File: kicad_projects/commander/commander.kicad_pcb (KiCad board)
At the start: 2 copper layers, 50 x 70 mm, 14 parts, among them J1 Conn_02x07_Odd_Even, J2 Conn_02x07_Odd_Even, J4 TPS pinout, J5 DS1020-12-6VBT1A-R, J6 PSP 3000 connector SFV4R-4STB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, J7 PSP 2000 raw pins out, U1 Pico, U2 FODM3053

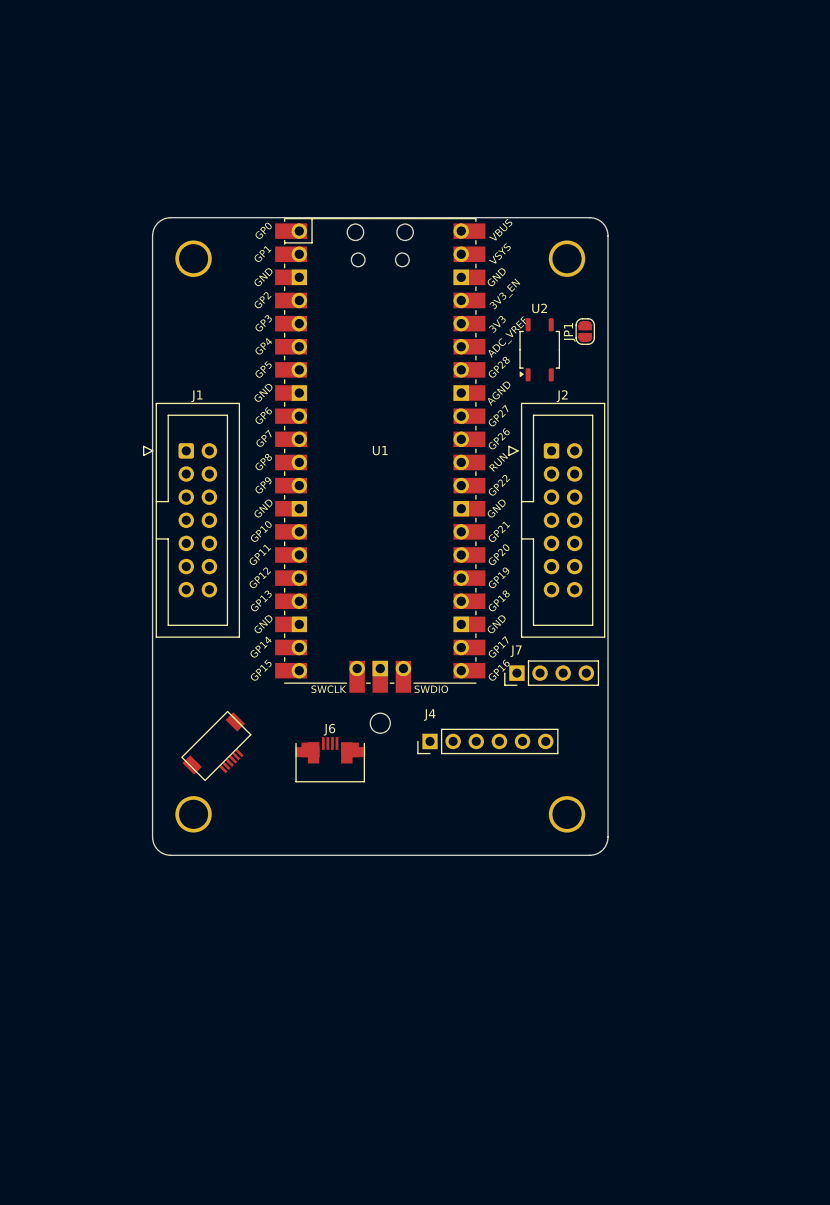
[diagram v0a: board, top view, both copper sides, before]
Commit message: Commander board passing DRC
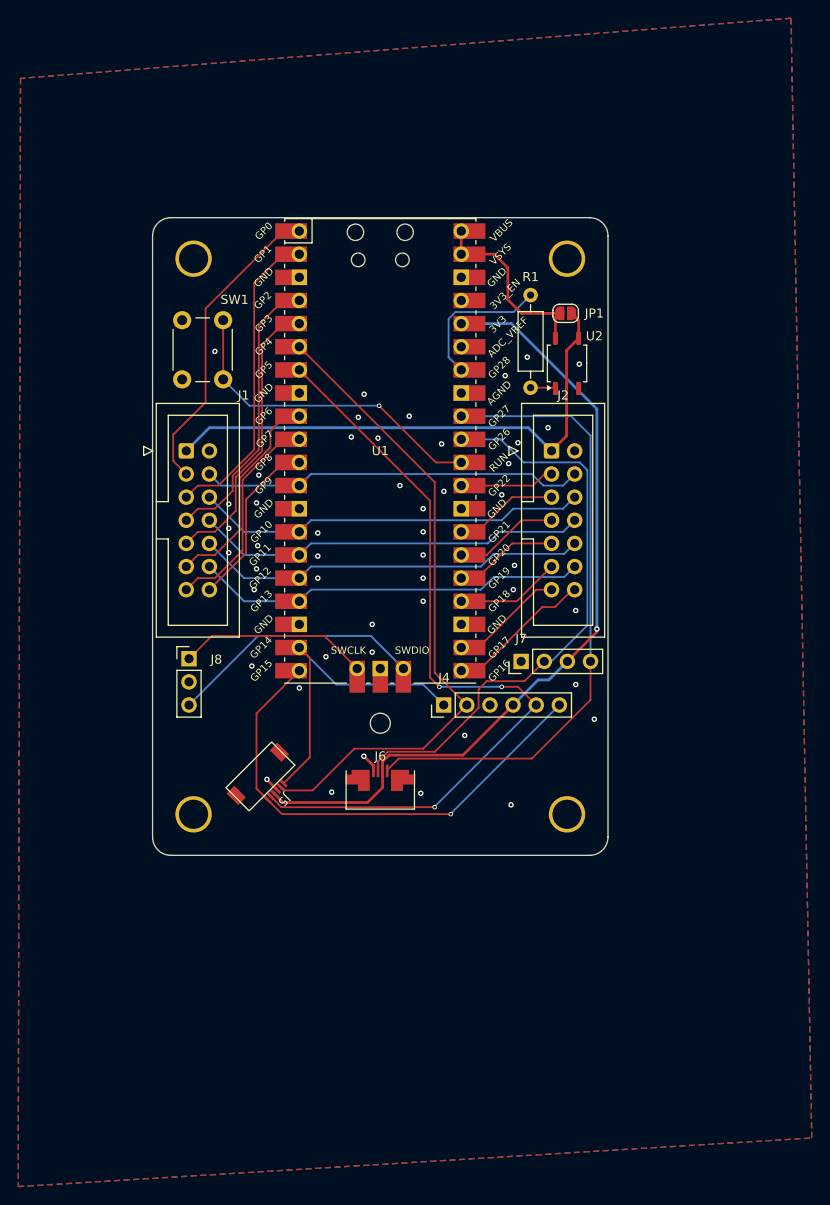
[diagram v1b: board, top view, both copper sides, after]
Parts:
- added J8: debug out, Connector_PinHeader_2.54mm:PinHeader_1x03_P2.54mm_Vertical, F.Cu at (114.0, 108.4)
- added R1: 200R, Resistor_THT:R_Axial_DIN0207_L6.3mm_D2.5mm_P10.16mm_Horizontal, F.Cu at (151.5, 78.7)
- added SW1: RESET_SWITCH, Button_Switch_THT:SW_PUSH_6mm_H4.3mm, F.Cu at (113.2, 77.8)
- J1: value Conn_02x07_Odd_Even -> left input IDC14
- J2: value Conn_02x07_Odd_Even -> right input IDC14
- U2: value FODM3053 -> AQY212S
- moved J6 6.26 mm to (135.0, 120.7)
- moved J5 5.88 mm to (123.5, 123.0)
- moved J4 4.27 mm to (142.0, 113.5)
- moved U2 3.35 mm to (155.5, 76.0)
- moved JP1 2.94 mm to (155.3, 70.5), turned to 0 degrees
- moved J7 1.37 mm to (150.5, 108.7)
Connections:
- J1 pad 1: unconnected-(J1-Pin_1-Pad1) -> LED_5V
- J1 pad 10: unconnected-(J1-Pin_10-Pad10) -> /ROW1
- J1 pad 11: unconnected-(J1-Pin_11-Pad11) -> /COL4
- J1 pad 12: unconnected-(J1-Pin_12-Pad12) -> /ROW0
- J1 pad 13: unconnected-(J1-Pin_13-Pad13) -> /COL5
- J1 pad 14: unconnected-(J1-Pin_14-Pad14) -> /COL6
- J1 pad 2: unconnected-(J1-Pin_2-Pad2) -> GND
- J1 pad 3: unconnected-(J1-Pin_3-Pad3) -> /COL0
- J1 pad 4: unconnected-(J1-Pin_4-Pad4) -> /ROW4
- J1 pad 5: unconnected-(J1-Pin_5-Pad5) -> /COL1
- J1 pad 6: unconnected-(J1-Pin_6-Pad6) -> /ROW3
- J1 pad 7: unconnected-(J1-Pin_7-Pad7) -> /COL2
- J1 pad 8: unconnected-(J1-Pin_8-Pad8) -> /ROW2
- J1 pad 9: unconnected-(J1-Pin_9-Pad9) -> /COL3
- J2 pad 1: unconnected-(J2-Pin_1-Pad1) -> LED_5V
- J2 pad 10: unconnected-(J2-Pin_10-Pad10) -> /ROW1
- J2 pad 11: unconnected-(J2-Pin_11-Pad11) -> /COL11
- J2 pad 12: unconnected-(J2-Pin_12-Pad12) -> /ROW0
- J2 pad 13: unconnected-(J2-Pin_13-Pad13) -> /COL12
- J2 pad 14: unconnected-(J2-Pin_14-Pad14) -> /COL13
- J2 pad 2: unconnected-(J2-Pin_2-Pad2) -> GND
- J2 pad 3: unconnected-(J2-Pin_3-Pad3) -> /COL7
- J2 pad 4: unconnected-(J2-Pin_4-Pad4) -> /ROW4
- J2 pad 5: unconnected-(J2-Pin_5-Pad5) -> /COL8
- J2 pad 6: unconnected-(J2-Pin_6-Pad6) -> /ROW3
- J2 pad 7: unconnected-(J2-Pin_7-Pad7) -> /COL9
- J2 pad 8: unconnected-(J2-Pin_8-Pad8) -> /ROW2
- J2 pad 9: unconnected-(J2-Pin_9-Pad9) -> /COL10
- JP1 pad 1: 5V5 -> 5V
- JP1 pad 2: LED_5V5 -> LED_5V
- U1 pad 1: unconnected-(U1-GPIO0-Pad1) -> /COL0
- U1 pad 10: unconnected-(U1-GPIO7-Pad10) -> /COL5
- U1 pad 11: unconnected-(U1-GPIO8-Pad11) -> /COL6
- U1 pad 12: unconnected-(U1-GPIO9-Pad12) -> /ROW4
- U1 pad 14: unconnected-(U1-GPIO10-Pad14) -> /ROW3
- U1 pad 15: unconnected-(U1-GPIO11-Pad15) -> /ROW2
- U1 pad 16: unconnected-(U1-GPIO12-Pad16) -> /ROW1
- U1 pad 17: unconnected-(U1-GPIO13-Pad17) -> /ROW0
- U1 pad 19: unconnected-(U1-GPIO14-Pad19) -> /TPS_RDY
- U1 pad 2: unconnected-(U1-GPIO1-Pad2) -> /COL1
- U1 pad 20: unconnected-(U1-GPIO15-Pad20) -> /TPS_NRST
- U1 pad 21: unconnected-(U1-GPIO16-Pad21) -> /COL13
- U1 pad 22: unconnected-(U1-GPIO17-Pad22) -> /COL12
- U1 pad 24: unconnected-(U1-GPIO18-Pad24) -> /COL11
- U1 pad 25: unconnected-(U1-GPIO19-Pad25) -> /COL10
- U1 pad 26: unconnected-(U1-GPIO20-Pad26) -> /COL9
- U1 pad 27: unconnected-(U1-GPIO21-Pad27) -> /COL8
- U1 pad 29: unconnected-(U1-GPIO22-Pad29) -> /COL7
- U1 pad 30: unconnected-(U1-RUN-Pad30) -> /RUN
- U1 pad 31: unconnected-(U1-GPIO26_ADC0-Pad31) -> /X1
- U1 pad 32: unconnected-(U1-GPIO27_ADC1-Pad32) -> /X2
- U1 pad 34: unconnected-(U1-GPIO28_ADC2-Pad34) -> /LED_ENABLE
- U1 pad 39: unconnected-(U1-VSYS-Pad39) -> 5V
- U1 pad 4: unconnected-(U1-GPIO2-Pad4) -> /COL2
- U1 pad 40: unconnected-(U1-VBUS-Pad40) -> 5V
- U1 pad 41: unconnected-(U1-SWCLK-Pad41) -> Net-(J8-Pin_1)
- U1 pad 43: unconnected-(U1-SWDIO-Pad43) -> Net-(J8-Pin_3)
- U1 pad 5: unconnected-(U1-GPIO3-Pad5) -> /COL3
- U1 pad 6: unconnected-(U1-GPIO4-Pad6) -> /TPS_SDA
- U1 pad 7: unconnected-(U1-GPIO5-Pad7) -> /TPS_SCL
- U1 pad 9: unconnected-(U1-GPIO6-Pad9) -> /COL4
- U2 pad 1: unconnected-(U2-Pad1) -> Net-(R1-Pad1)
- U2 pad 2: unconnected-(U2-Pad2) -> GND
- U2 pad 3: LED_5V5 -> LED_5V
- U2 pad 4: 5V5 -> 5V
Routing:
- net 3V3: track 0.00 -> 88.5 mm, vias 0 -> 1
- net /TPS_SCL: track 0.00 -> 87.0 mm, vias 0 -> 3
- net /TPS_SDA: track 0.00 -> 71.5 mm
- net /X2: track 0.00 -> 70.5 mm
- net /X1: track 0.00 -> 64.0 mm
- net LED_5V: track 0.00 -> 58.9 mm
- net /TPS_NRST: track 0.00 -> 54.3 mm, vias 0 -> 1
- net /ROW2: track 0.00 -> 43.3 mm
- net /ROW0: track 0.00 -> 43.3 mm
- net /ROW3: track 0.00 -> 43.3 mm
- net /ROW1: track 0.00 -> 43.3 mm
- net /ROW4: track 0.00 -> 42.2 mm
- net /RUN: track 0.00 -> 36.4 mm, vias 0 -> 1
- net /TPS_RDY: track 0.00 -> 35.1 mm
- net /COL1: track 0.00 -> 34.2 mm
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- added copper zone on B.Cu, net GND
- added copper zone on F.Cu, net GND

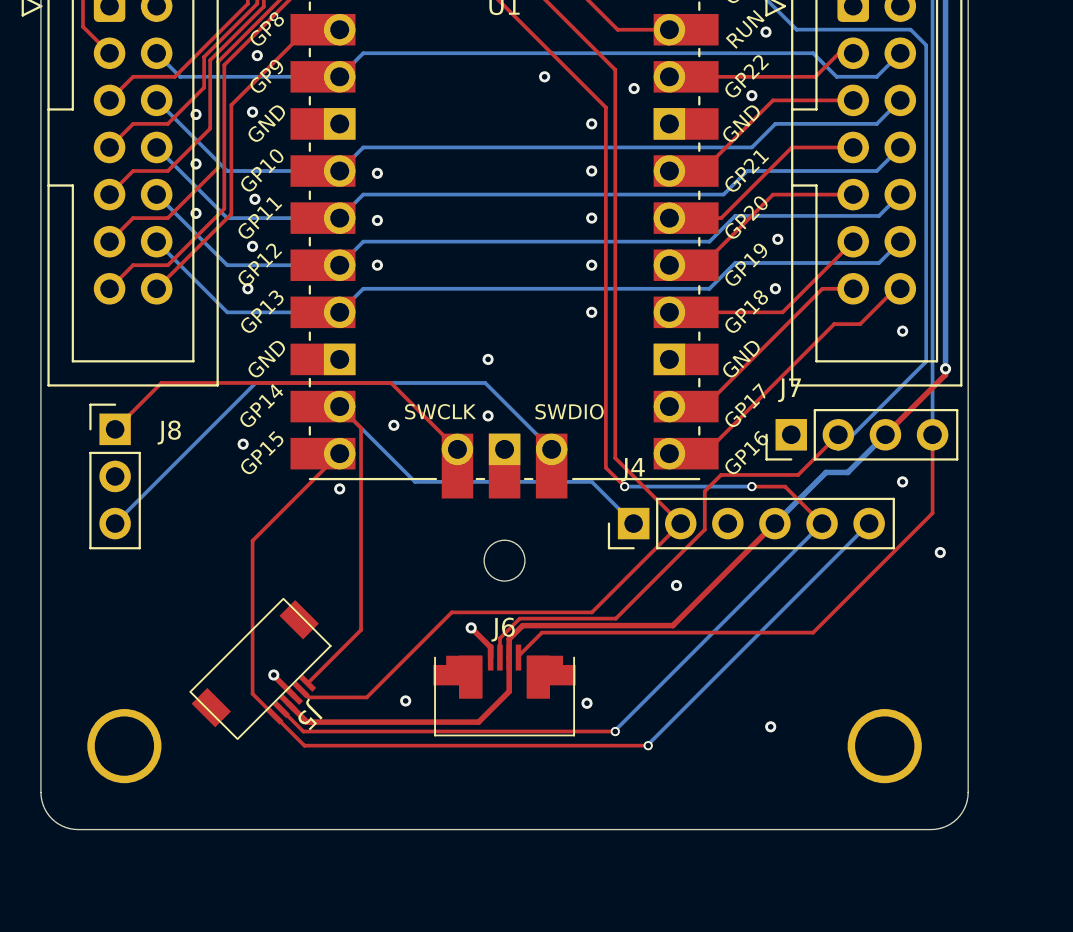
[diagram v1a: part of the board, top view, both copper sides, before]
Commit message: Add silkscreen info, some more routing
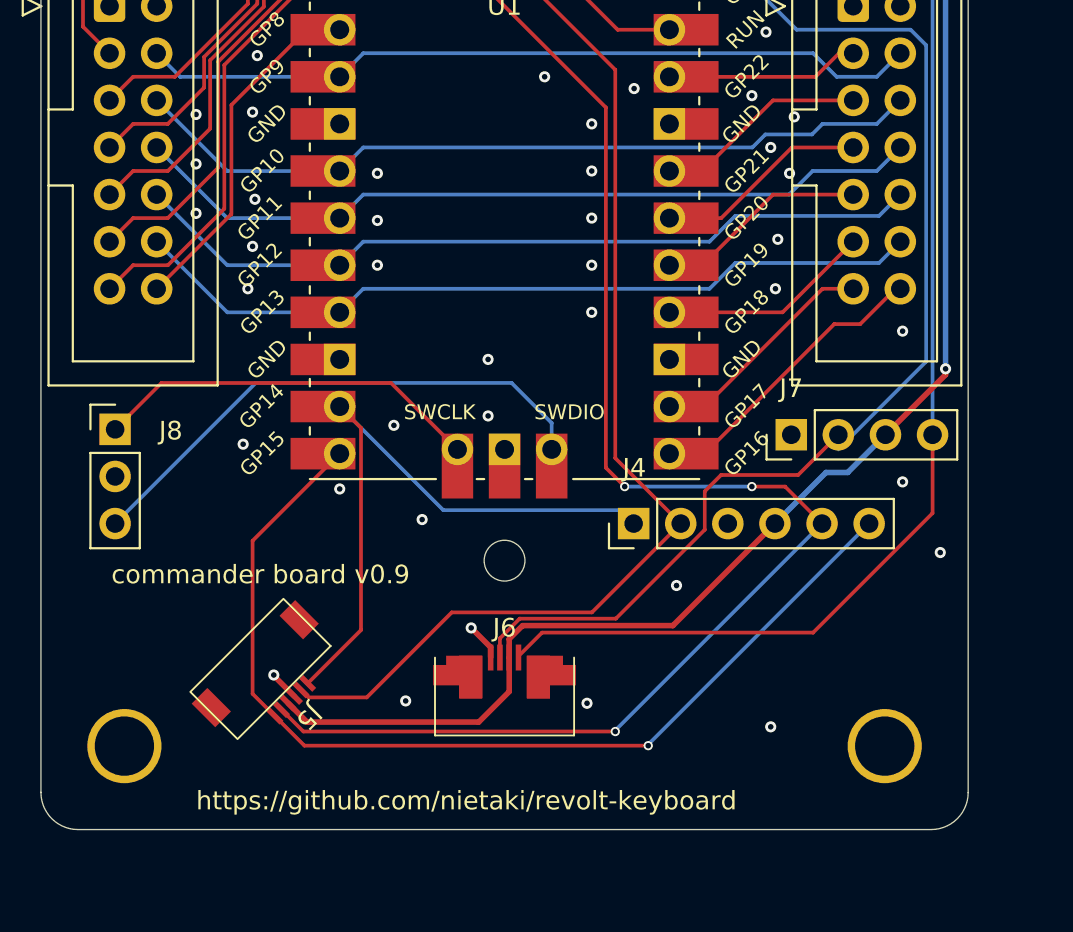
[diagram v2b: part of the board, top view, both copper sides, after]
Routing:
- net Net-(J8-Pin_3): track 28.2 -> 29.0 mm
- net GND: vias 48 -> 52
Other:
- board text added: "commander board v0.9"
- board text added: "https://github.com/nietaki/revolt-keyboard"
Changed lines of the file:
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@@
   (gr_line (start 160 62) (end 160 128)
     (stroke (width 0.05) (type default)) (layer "Edge.Cuts"))
+  (gr_text "https://github.com/nietaki/revolt-keyboard" (at 118.364 129.032) (layer "F.SilkS")
+    (effects (font (size 1 1) (thickness 0.15)) (justify left bottom))
+  )
+  (gr_text "commander board v0.9" (at 113.792 116.84) (layer "F.SilkS")
+    (effects (font (size 1 1) (thickness 0.15)) (justify left bottom))
+  )
   (gr_text "PSP joystick" (at 130.5 130.5) (layer "Dwgs.User")
     (effects (font (size 1 1) (thickness 0.15)) (justify left bottom))
@@
   (segment (start 121.158 85.471) (end 117.221 89.408) (width 0.2) (layer "F.Cu") (net 3))
   (segment (start 121.158 67.183) (end 121.158 85.471) (width 0.2) (layer "F.Cu") (net 3))
-  (segment (start 149.606 91.948) (end 148.336 93.218) (width 0.2) (layer "B.Cu") (net 4))
+  (segment (start 151.576 92.518) (end 149.06205 92.518) (width 0.2) (layer "B.Cu") (net 4))
+  (segment (start 127.382 93.218) (end 126.11 94.49) (width 0.2) (layer "B.Cu") (net 4))
+  (segment (start 149.06205 92.518) (end 148.36205 93.218) (width 0.2) (layer "B.Cu") (net 4))
+  (segment (start 155.072 91.948) (end 152.146 91.948) (width 0.2) (layer "B.Cu") (net 4))
+  (segment (start 152.146 91.948) (end 151.576 92.518) (width 0.2) (layer "B.Cu") (net 4))
   (segment (start 156.34 90.68) (end 155.072 91.948) (width 0.2) (layer "B.Cu") (net 4))
   (segment (start 126.11 94.49) (end 120.05 94.49) (width 0.2) (layer "B.Cu") (net 4))
   (segment (start 120.05 94.49) (end 116.24 90.68) (width 0.2) (layer "B.Cu") (net 4))
-  (segment (start 127.382 93.218) (end 126.11 94.49) (width 0.2) (layer "B.Cu") (net 4))
-  (segment (start 148.336 93.218) (end 127.382 93.218) (width 0.2) (layer "B.Cu") (net 4))
-  (segment (start 155.072 91.948) (end 149.606 91.948) (width 0.2) (layer "B.Cu") (net 4))
+  (segment (start 148.36205 93.218) (end 127.382 93.218) (width 0.2) (layer "B.Cu") (net 4))
   (segment (start 118.799 89.989) (end 116.84 91.948) (width 0.2) (layer "F.Cu") (net 5))
   (segment (start 126.11 69.09) (end 124.331 69.09) (width 0.2) (layer "F.Cu") (net 5))
@@
   (segment (start 116.84 91.948) (end 114.972 91.948) (width 0.2) (layer "F.Cu") (net 5))
   (segment (start 121.666 71.755) (end 121.666 85.471) (width 0.2) (layer "F.Cu") (net 5))
+  (segment (start 127.382 95.758) (end 126.11 97.03) (width 0.2) (layer "B.Cu") (net 6))
+  (segment (start 151.61195 94.488) (end 150.34195 95.758) (width 0.2) (layer "B.Cu") (net 6))
+  (segment (start 150.34195 95.758) (end 127.382 95.758) (width 0.2) (layer "B.Cu") (net 6))
+  (segment (start 120.05 97.03) (end 116.24 93.22) (width 0.2) (layer "B.Cu") (net 6))
+  (segment (start 155.072 94.488) (end 151.61195 94.488) (width 0.2) (layer "B.Cu") (net 6))
   (segment (start 156.34 93.22) (end 155.072 94.488) (width 0.2) (layer "B.Cu") (net 6))
-  (segment (start 148.082 94.488) (end 146.812 95.758) (width 0.2) (layer "B.Cu") (net 6))
-  (segment (start 120.05 97.03) (end 116.24 93.22) (width 0.2) (layer "B.Cu") (net 6))
-  (segment (start 146.812 95.758) (end 127.382 95.758) (width 0.2) (layer "B.Cu") (net 6))
-  (segment (start 155.072 94.488) (end 148.082 94.488) (width 0.2) (layer "B.Cu") (net 6))
   (segment (start 126.11 97.03) (end 120.05 97.03) (width 0.2) (layer "B.Cu") (net 6))
-  (segment (start 127.382 95.758) (end 126.11 97.03) (width 0.2) (layer "B.Cu") (net 6))
   (segment (start 122.018478 73.942522) (end 124.331 71.63) (width 0.2) (layer "F.Cu") (net 7))
   (segment (start 116.84 94.488) (end 119.126 92.202) (width 0.2) (layer "F.Cu") (net 7))
@@
   (segment (start 132.46 109.5) (end 128.878 105.918) (width 0.2) (layer "F.Cu") (net 20))
   (segment (start 116.502 105.918) (end 114 108.42) (width 0.2) (layer "F.Cu") (net 20))
-  (segment (start 133.958 105.918) (end 121.582 105.918) (width 0.2) (layer "B.Cu") (net 21))
   (segment (start 121.582 105.918) (end 114 113.5) (width 0.2) (layer "B.Cu") (net 21))
-  (segment (start 137.54 109.5) (end 133.958 105.918) (width 0.2) (layer "B.Cu") (net 21))
+  (segment (start 137.54 108.076) (end 135.382 105.918) (width 0.2) (layer "B.Cu") (net 21))
+  (segment (start 137.54 109.5) (end 137.54 108.076) (width 0.2) (layer "B.Cu") (net 21))
+  (segment (start 135.382 105.918) (end 121.582 105.918) (width 0.2) (layer "B.Cu") (net 21))
   (segment (start 117.75 71.25) (end 117.75 77.75) (width 0.2) (layer "F.Cu") (net 22))
   (segment (start 134.874 80.645) (end 141.099 86.87) (width 0.2) (layer "F.Cu") (net 22))
@@
   (segment (start 127.26 119.24) (end 124.383883 122.116117) (width 0.2) (layer "F.Cu") (net 27))
   (segment (start 126.11 107.19) (end 127.26 108.34) (width 0.2) (layer "F.Cu") (net 27))
-  (segment (start 139.712 111.252) (end 141.96 113.5) (width 0.2) (layer "B.Cu") (net 27))
-  (segment (start 130.172 111.252) (end 139.712 111.252) (width 0.2) (layer "B.Cu") (net 27))
-  (segment (start 126.11 107.19) (end 130.172 111.252) (width 0.2) (layer "B.Cu") (net 27))
+  (segment (start 126.11 107.19) (end 131.696 112.776) (width 0.2) (layer "B.Cu") (net 27))
+  (segment (start 131.696 112.776) (end 141.236 112.776) (width 0.2) (layer "B.Cu") (net 27))
+  (segment (start 141.236 112.776) (end 141.96 113.5) (width 0.2) (layer "B.Cu") (net 27))
   (segment (start 127.568264 122.875736) (end 124.436396 122.875736) (width 0.2) (layer "F.Cu") (net 28))
   (segment (start 124.436396 122.875736) (end 124.03033 122.46967) (width 0.2) (layer "F.Cu") (net 28))
@@
   (via (at 156.464 111.252) (size 0.6) (drill 0.3) (layers "F.Cu" "B.Cu") (net 29))
   (via (at 158.496 115.062) (size 0.6) (drill 0.3) (layers "F.Cu" "B.Cu") (net 29))
+  (via (at 150.368 94.615) (size 0.6) (drill 0.3) (layers "F.Cu" "B.Cu") (net 29))
   (via (at 139.7 97.028) (size 0.6) (drill 0.3) (layers "F.Cu" "B.Cu") (net 29))
   (via (at 126.111 111.633) (size 0.6) (drill 0.3) (layers "F.Cu" "B.Cu") (net 29))
@@
   (via (at 148.717 77.343) (size 0.6) (drill 0.3) (layers "F.Cu" "B.Cu") (net 29))
   (via (at 121.539 96.012) (size 0.6) (drill 0.3) (layers "F.Cu" "B.Cu") (net 29))
+  (via (at 130.556 113.284) (size 0.6) (drill 0.3) (layers "F.Cu" "B.Cu") (net 29))
   (via (at 149.098 86.995) (size 0.6) (drill 0.3) (layers "F.Cu" "B.Cu") (net 29))
   (via (at 128.143 94.615) (size 0.6) (drill 0.3) (layers "F.Cu" "B.Cu") (net 29))
@@
   (via (at 128.143 99.568) (size 0.6) (drill 0.3) (layers "F.Cu" "B.Cu") (net 29))
   (via (at 121.666 88.265) (size 0.6) (drill 0.3) (layers "F.Cu" "B.Cu") (net 29))
+  (via (at 149.352 93.218) (size 0.6) (drill 0.3) (layers "F.Cu" "B.Cu") (net 29))
   (via (at 133.201 119.126) (size 0.6) (drill 0.3) (layers "F.Cu" "B.Cu") (net 29))
   (via (at 121.158 100.838) (size 0.6) (drill 0.3) (layers "F.Cu" "B.Cu") (net 29))
+  (via (at 150.622 91.567) (size 0.6) (drill 0.3) (layers "F.Cu" "B.Cu") (net 29))
   (via (at 133.223 79.375) (size 0.6) (drill 0.3) (layers "F.Cu" "B.Cu") (net 29))
   (via (at 153.416 83.058) (size 0.6) (drill 0.3) (layers "F.Cu" "B.Cu") (net 29))
